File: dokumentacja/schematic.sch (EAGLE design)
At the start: 11 parts

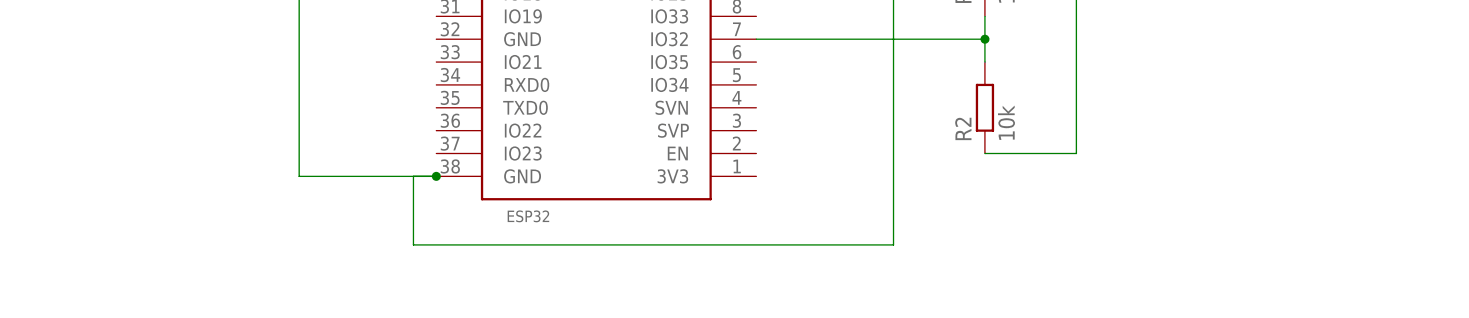
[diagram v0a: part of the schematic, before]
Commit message: Added PDF of the schematic
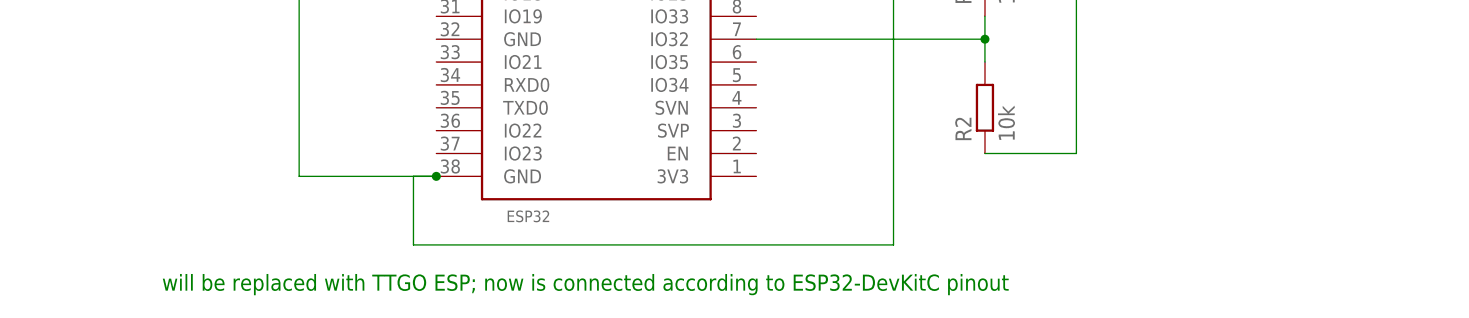
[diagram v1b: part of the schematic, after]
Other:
- note added: "will be replaced with TTGO ESP; now is connected according to ESP32-DevKitC pinout"
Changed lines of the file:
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@@
 <text x="93.98" y="20.32" size="1.778" layer="91">~230V, 50Hz</text>
 <text x="-68.58" y="5.08" size="1.778" layer="91">~230V, 50Hz</text>
+<text x="-48.26" y="-35.56" size="1.778" layer="91">will be replaced with TTGO ESP; now is connected according to ESP32-DevKitC pinout</text>
 </plain>
 <instances>
